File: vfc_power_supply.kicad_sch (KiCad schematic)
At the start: 23 parts, among them J1 Conn_02x08_Odd_Even, J2 Conn_01x02_Male, J3 Conn_01x03_Male, M1 Logo_10mmx10mm, P1 Conn_02x20_Odd_Even

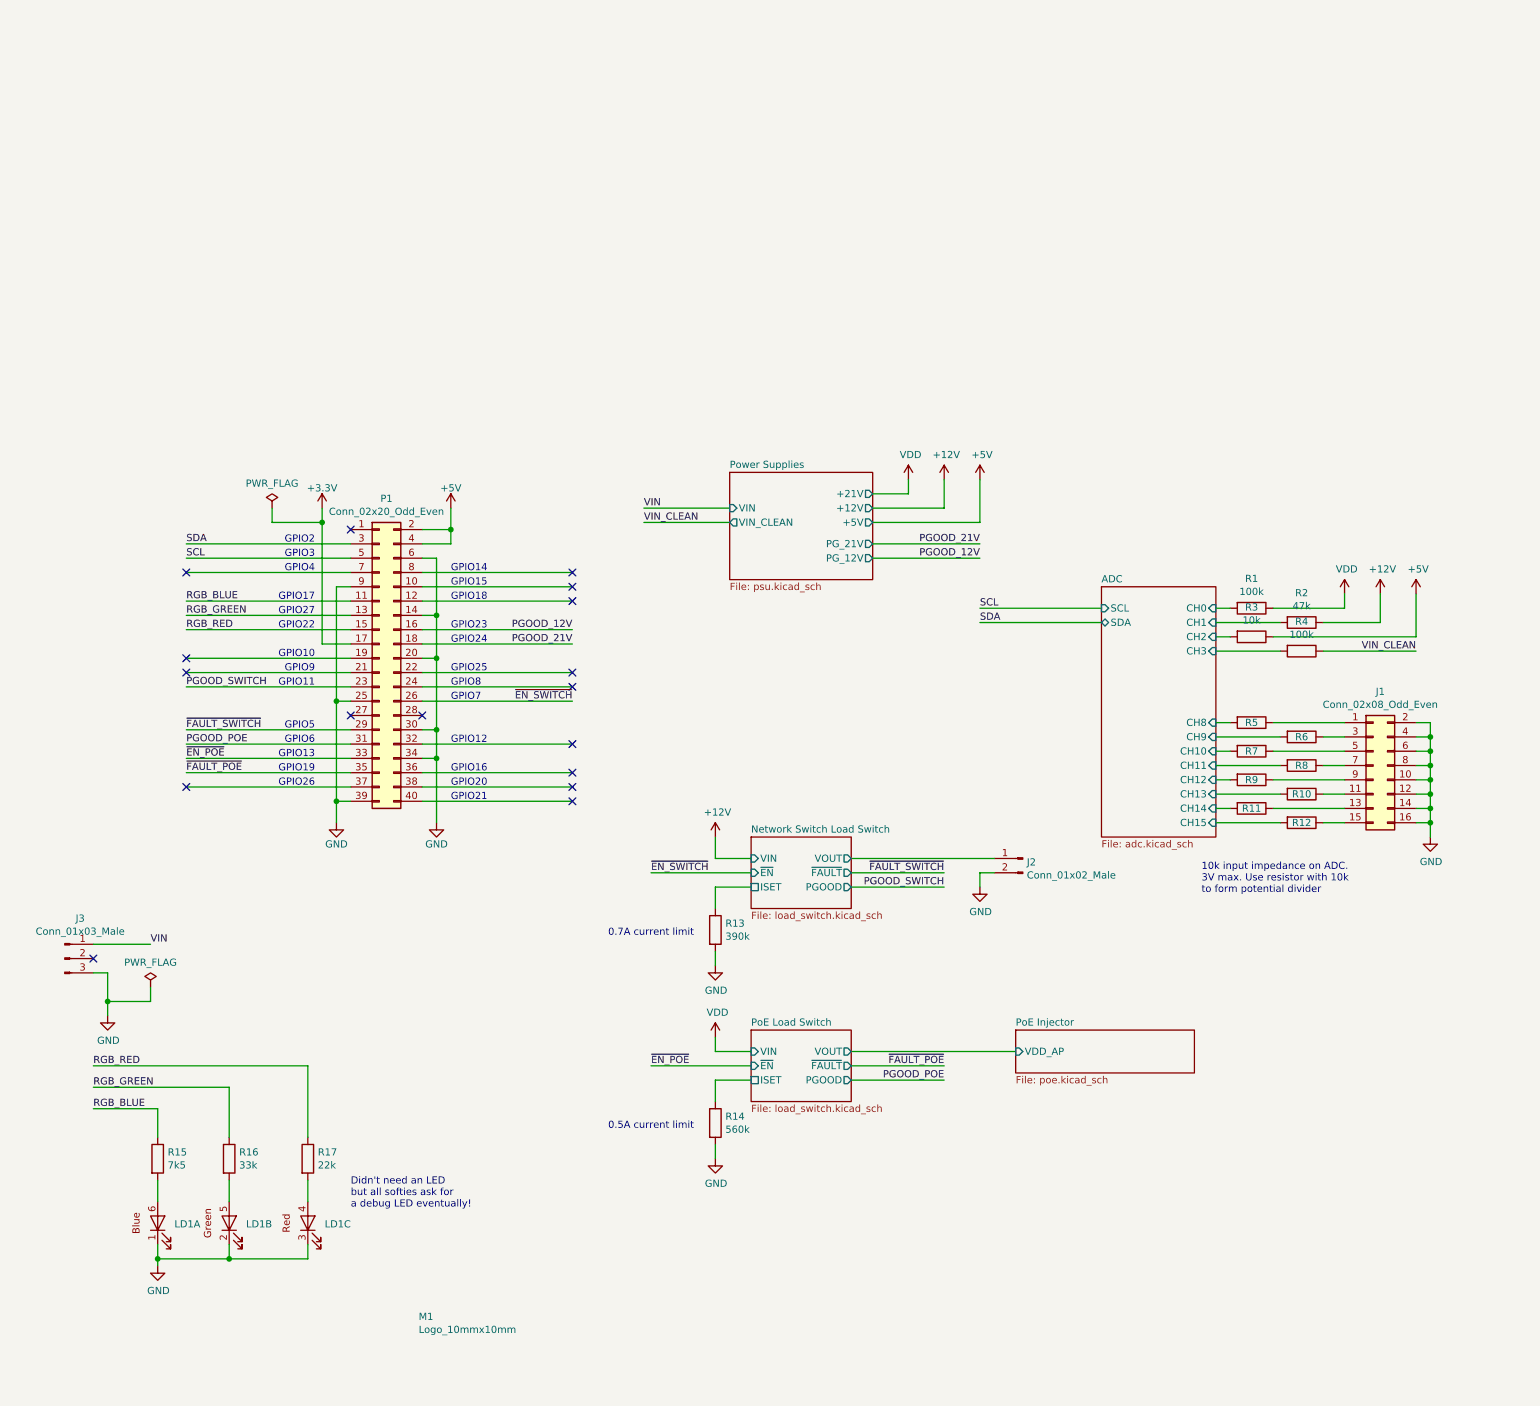
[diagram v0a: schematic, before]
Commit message: Updated library parts
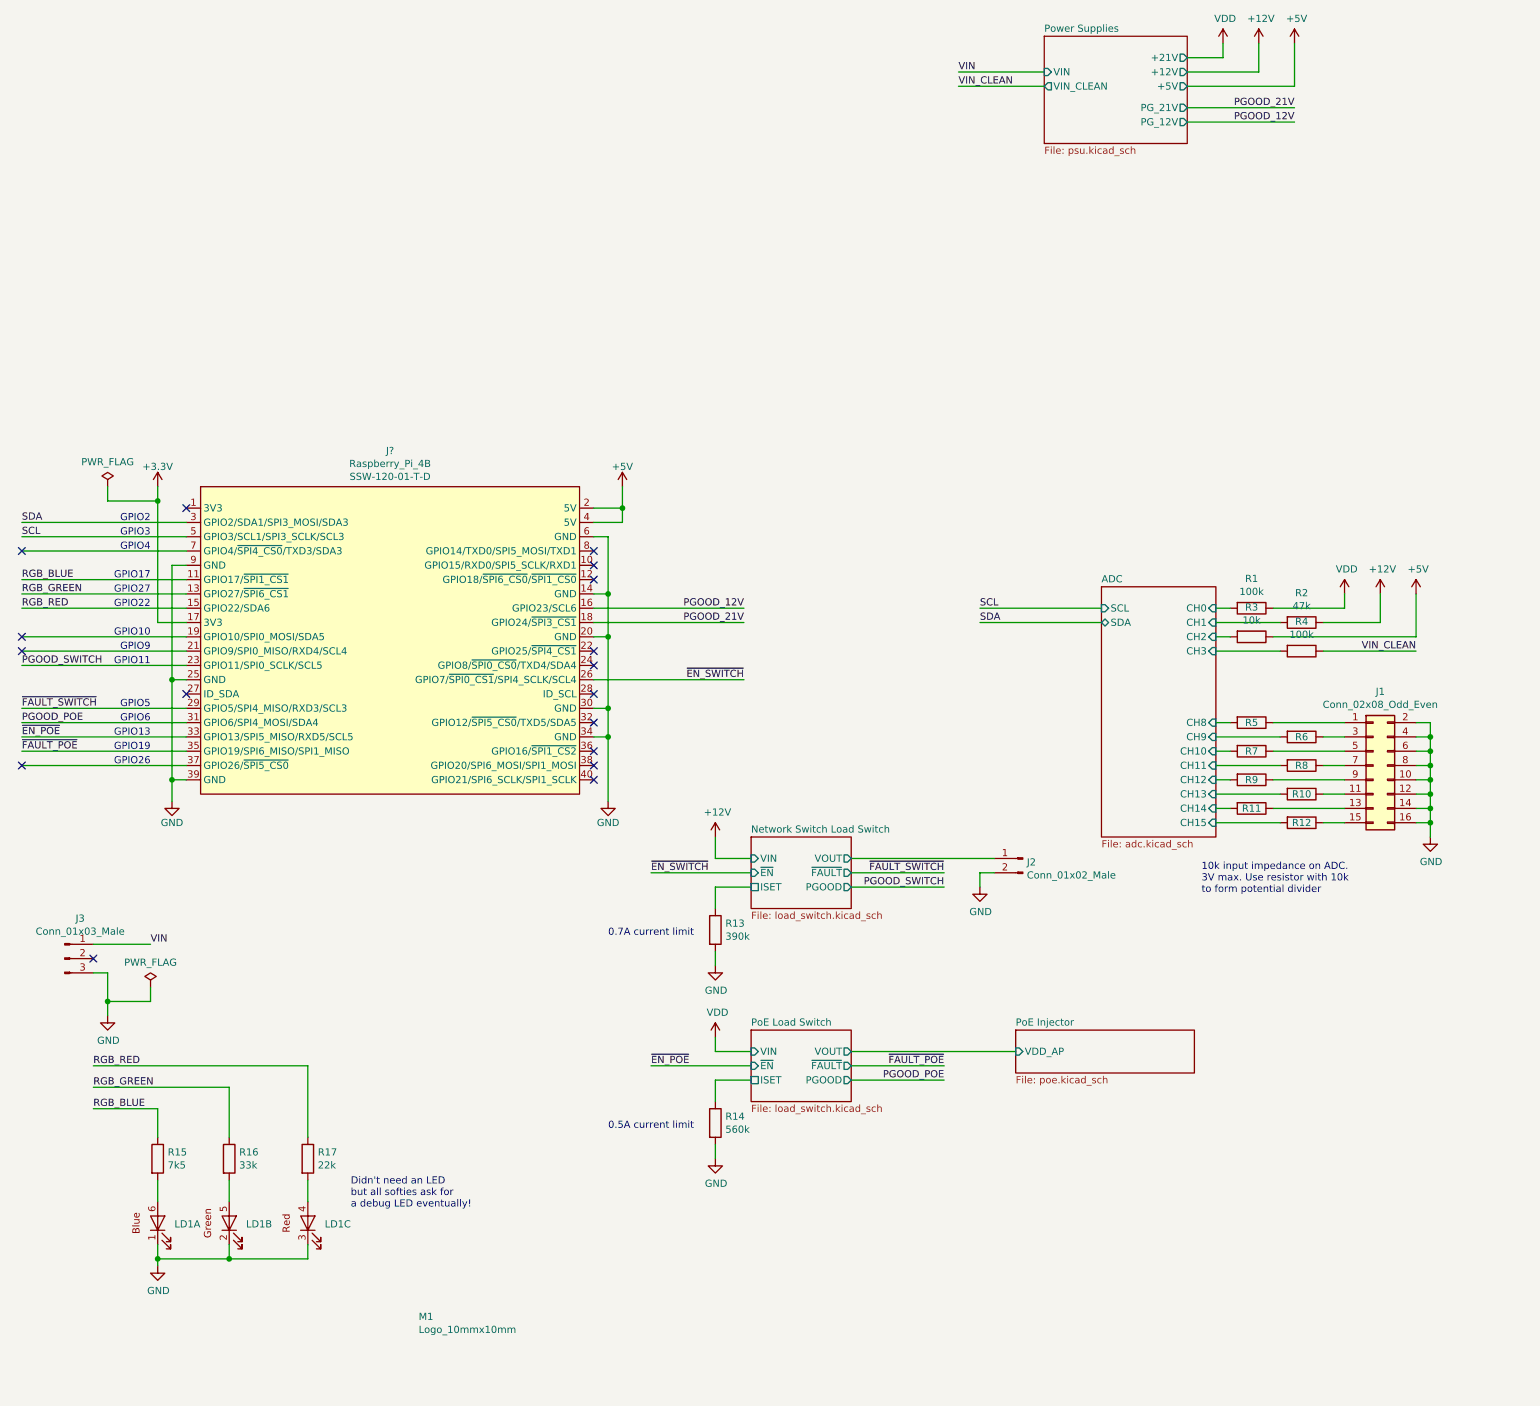
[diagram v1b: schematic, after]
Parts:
- removed P1: Conn_02x20_Odd_Even, Connector_PinSocket_2.54mm:PinSocket_2x20_P2.54mm_Vertical, symbol Connector_Generic:Conn_02x20_Odd_Even
- added J?: Raspberry_Pi_4B, Modules_WUT:Pi4, symbol Modules_WUT:Raspberry_Pi_4B
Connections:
- net +3V3: now also J?.17 (3V3)
- net +5V: now also J?.2 (5V), J?.4 (5V)
- net GND: now also J?.14 (GND), J?.20 (GND), J?.25 (GND), J?.30 (GND), J?.34 (GND), J?.39 (GND), J?.6 (GND), J?.9 (GND)
- net PGOOD_12V: now also J?.16 (GPIO23/SCL6)
- net PGOOD_21V: now also J?.18 (GPIO24/~SPI3_CS1~)
- net PGOOD_POE: now also J?.31 (GPIO6/SPI4_MOSI/SDA4)
- net PGOOD_SWITCH: now also J?.23 (GPIO11/SPI0_SCLK/SCL5)
- net RGB_BLUE: now also J?.11 (GPIO17/~SPI1_CS1~)
- net RGB_GREEN: now also J?.13 (GPIO27/~SPI6_CS1)
- net RGB_RED: now also J?.15 (GPIO22/SDA6)
- net SCL: now also J?.5 (GPIO3/SCL1/SPI3_SCLK/SCL3)
- net SDA: now also J?.3 (GPIO2/SDA1/SPI3_MOSI/SDA3)
- net ~EN_POE: now also J?.33 (GPIO13/SPI5_MISO/RXD5/SCL5)
- net ~EN_SWITCH: now also J?.26 (GPIO7/~SPI0_CS1~/SPI4_SCLK/SCL4)
- net ~FAULT_POE: now also J?.35 (GPIO19/SPI6_MISO/SPI1_MISO)
- net ~FAULT_SWITCH: now also J?.29 (GPIO5/SPI4_MISO/RXD3/SCL3)
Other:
- note removed: "GPIO12"
- note removed: "GPIO14"
- note removed: "GPIO15"
- note removed: "GPIO16"
- note removed: "GPIO18"
- note removed: "GPIO20"
- note removed: "GPIO21"
- note removed: "GPIO23"
- note removed: "GPIO24"
- note removed: "GPIO25"
- note removed: "GPIO7"
- note removed: "GPIO8"

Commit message: new layout
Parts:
- J6: renamed from J?; footprint Modules_WUT:Pi4 -> Modules_WUT:Raspberry_Pi_4B

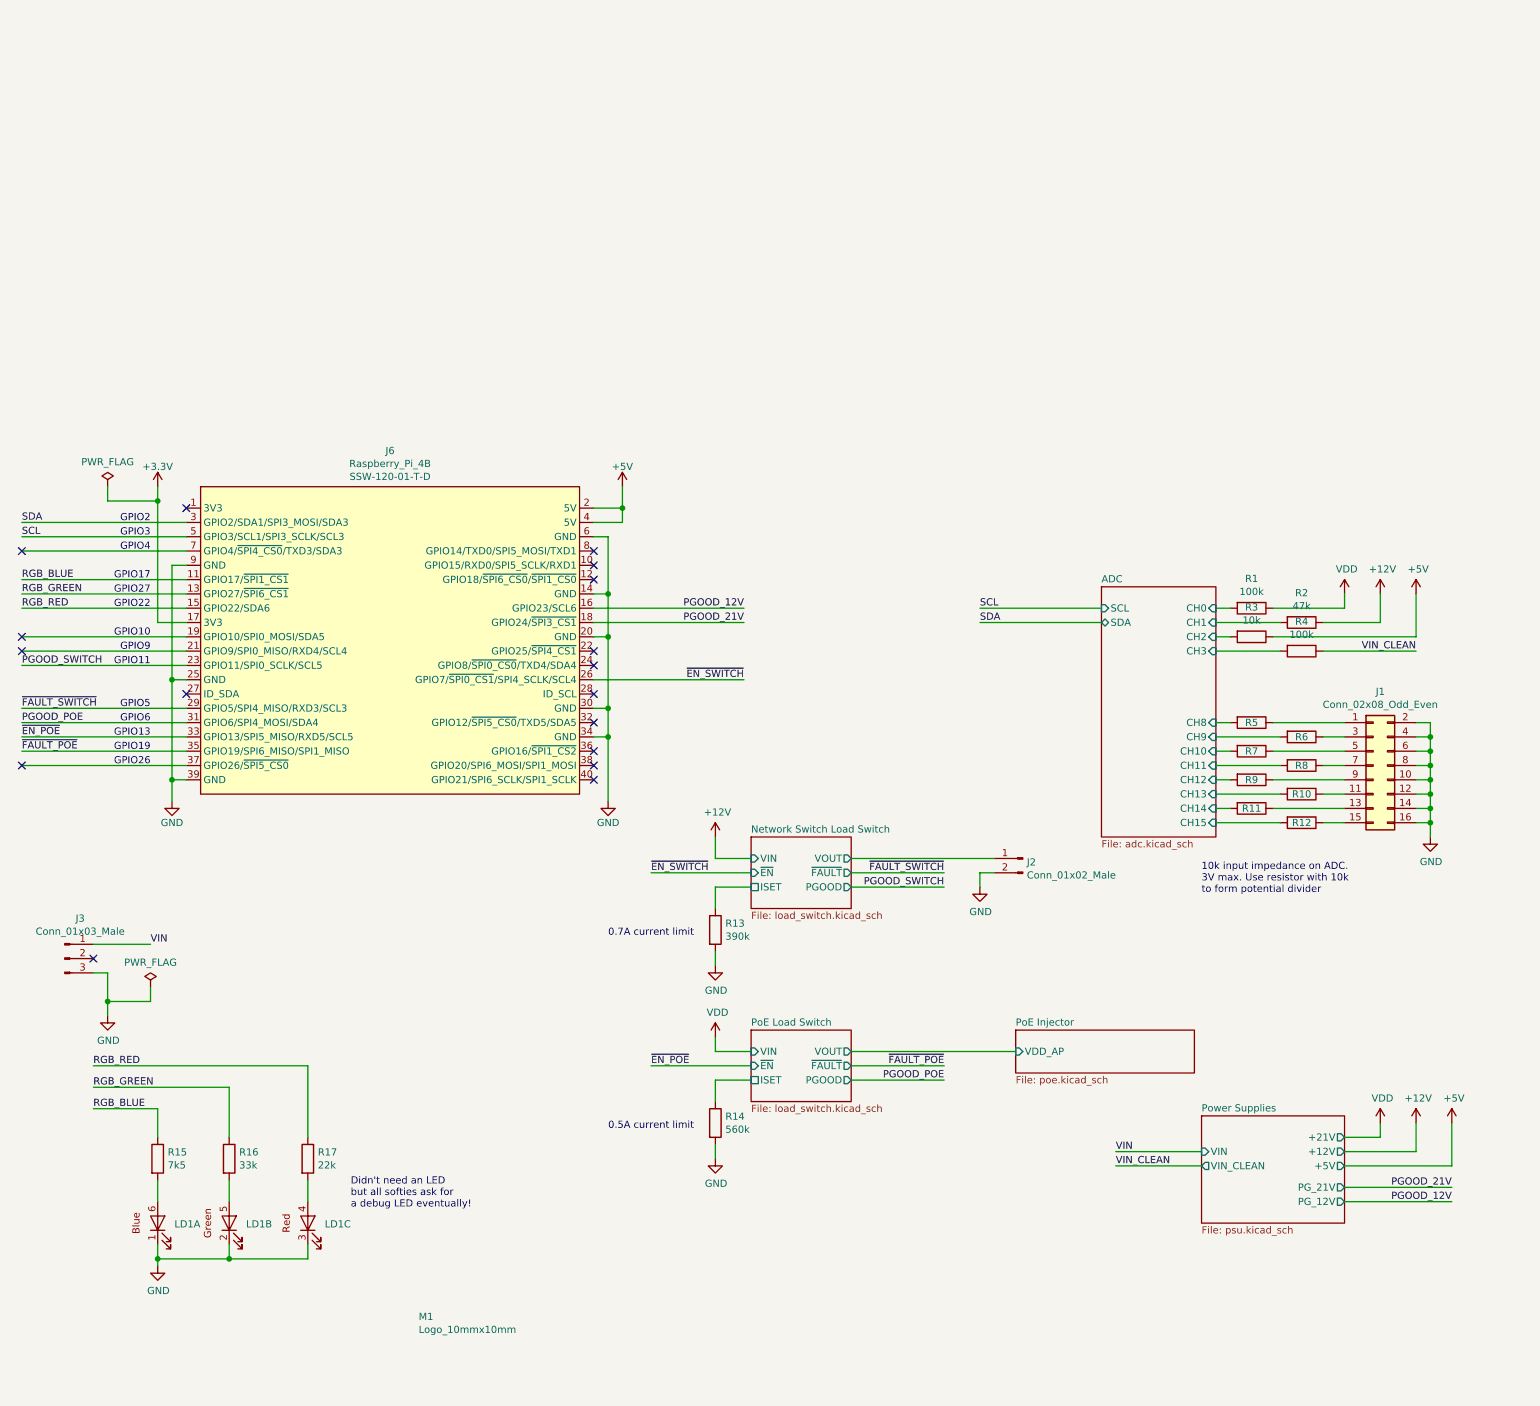
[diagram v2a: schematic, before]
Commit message: Started new connector layout
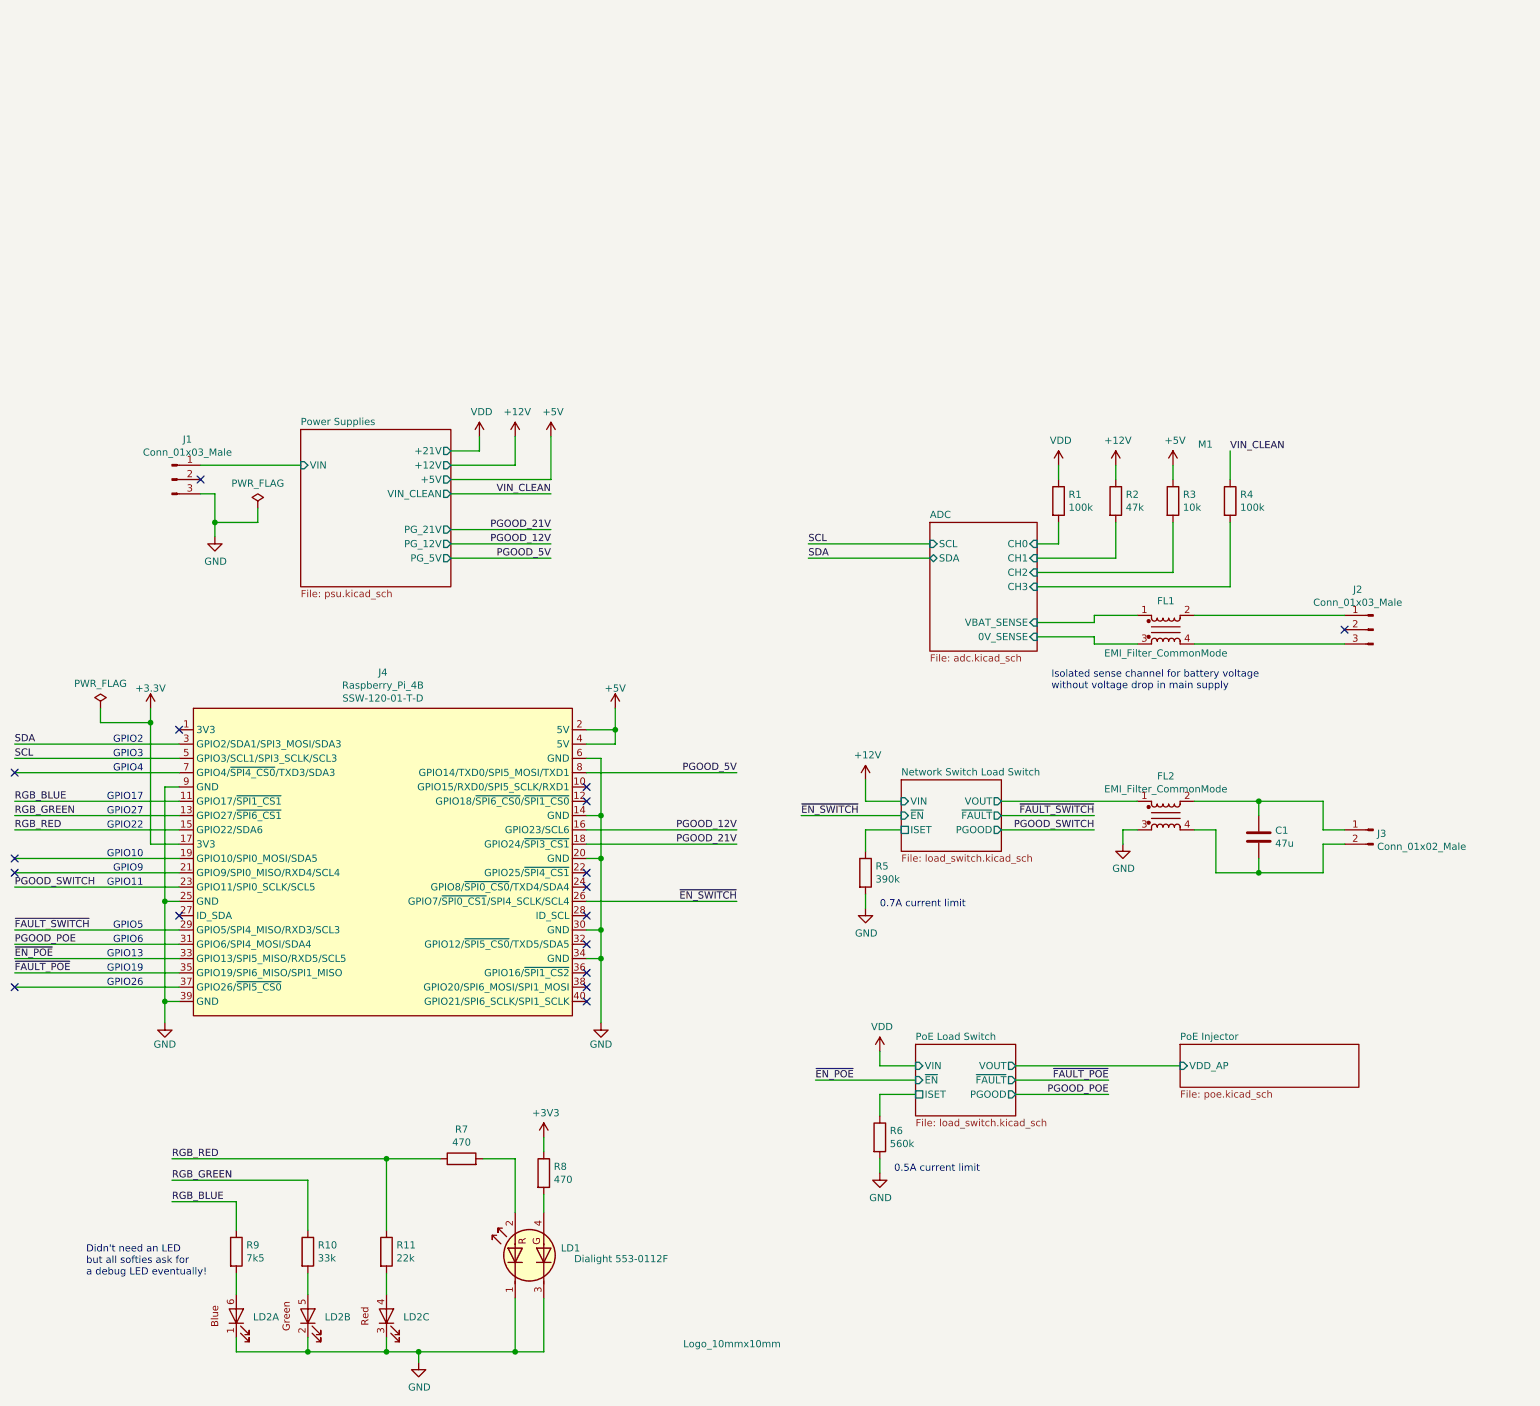
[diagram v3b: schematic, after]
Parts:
- removed J1: Conn_02x08_Odd_Even, Connector_PinHeader_2.54mm:PinHeader_2x08_P2.54mm_Vertical, symbol Connector_Generic:Conn_02x08_Odd_Even
- removed R10, R11, R12, R5, R6, R9: R, Resistor_SMD:R_0402_1005Metric, symbol Device:R
- added C1: 47u, Capacitor_SMD:C_1206_3216Metric, symbol Device:C
- added FL1, FL2: EMI_Filter_CommonMode, Inductor_WUT:TDK_ACM7060-301-2PL-TL01, symbol Device:EMI_Filter_CommonMode
- added J2: Conn_01x03_Male, Connector_WUT:Powerpole_PP30-with-1377G2-PCB-pins-25A_3WAY, symbol Connector:Conn_01x03_Male
- added LD1: Dialight 553-0112F, LED_WUT:LED_Dialight_553-0112F, symbol LED_WUT:LED_Dialight_553-0112F
- J3: renamed from J2; footprint Connector_Molex:Molex_KK-254_AE-6410-02A_1x02_P2.54mm_Vertical -> Connector_WUT:Weidmuller_SL3.5-2-90G
- R7, R8: value R -> 470
- renumbered J3 to J1, J6 to J4, LD1 to LD2, R16 to R10, R17 to R11, R13 to R5, R14 to R6, R15 to R9
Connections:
- net +3V3: now also R8.1
- net GND: now also FL2.3, LD1.1, LD1.3; no longer J3.2 (Pin_2)
- net Network Switch Load Switch/VOUT: now also FL2.1; no longer J3.1 (Pin_1)
- net RGB_RED: now also R7.1
- net PGOOD_5V: now reaches J4.8 (GPIO14/TXD0/SPI5_MOSI/TXD1)
- net ADC/CH10: no longer names the net of R7.2
- net ADC/CH10: now also LD1.2
- net ADC/CH11: no longer names the net of R8.2
- net ADC/CH11: now also LD1.4
- net VIN renamed Power Supplies/VIN
- new net: C1.1, FL2.2, J3.1 (Pin_1)
- new net: C1.2, FL2.4, J3.2 (Pin_2)
- new net: FL1.2, J2.1 (Pin_1)
- new net: FL1.4, J2.3 (Pin_3)
- new net ADC/0V_SENSE: FL1.3
- new net ADC/VBAT_SENSE: FL1.1
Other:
- sheet ADC ports: added 0V_SENSE, VBAT_SENSE; removed CH10, CH11, CH12, CH13, CH14, CH15, CH8, CH9
- sheet Power Supplies ports: added PG_5V; removed none
- note added: "Isolated sense channel for battery voltage without voltage drop in main supply"
- note removed: "10k input impedance on ADC. 3V max. Use resistor with 10k to form potential divider"
- moved on the sheet: J1, J3, J4, LD2A, LD2B, LD2C, R10, R11, R5, R6, R9
